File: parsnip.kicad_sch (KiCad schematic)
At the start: 67 parts, among them J1 SPI BUS, J2 I2C3, J3 I2C1, J4 I2C2, J5 e-Ink Display Connector, J6 UART0, SW1 ESP_RESET, SW2 BOOT, U1 ESP32-S3-WROOM-1-N16R8, Y1 32.768KHz

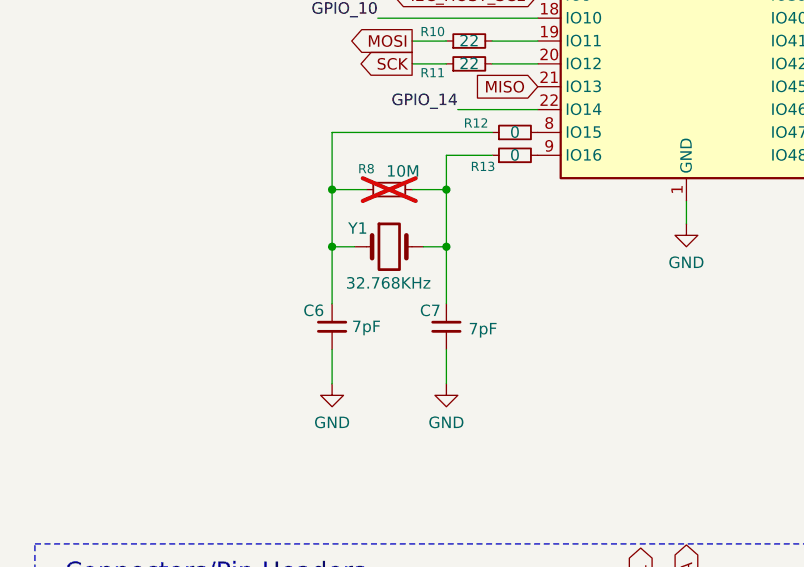
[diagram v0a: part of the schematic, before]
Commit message: organize part fields
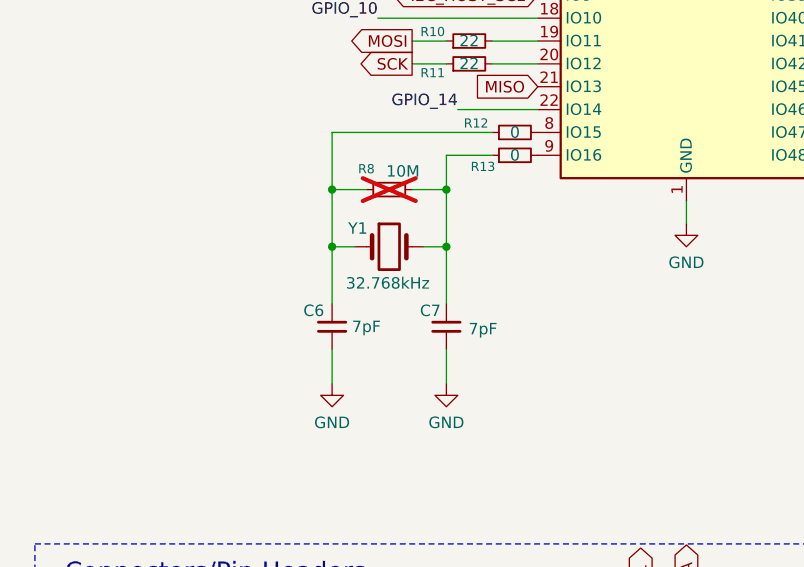
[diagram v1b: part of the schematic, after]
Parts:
- C1, C2, C3, C8: Capacitor Rating X5R -> (none); Dielectric (none) -> X5R; MPN (none) -> HGC0402R5225K350NTEJ; Manufacturer (none) -> Chinocera; Tolerance (none) -> 10%; Voltage Rating 25V -> 35V
- C10, C11: Capacitor Rating X7R -> (none); Dielectric (none) -> X5R; MPN (none) -> TCC0603X5R106M350CT; Manufacturer (none) -> CCTC; Tolerance (none) -> 20%; Voltage Rating 16V -> 35V
- C13: Dielectric (none) -> X5R; MPN (none) -> HGC0402R5225K350NTEJ; Manufacturer (none) -> Chinocera; Tolerance (none) -> 10%; Voltage Rating 16V -> 35V
- C14: Dielectric (none) -> X5R; MPN (none) -> CGA0805X5R106M500MT; Manufacturer (none) -> HRE; Tolerance (none) -> 20%; Voltage Rating 25V -> 50V
- C17: Dielectric (none) -> X7R; MPN (none) -> TCC0402X7R105K250AT; Manufacturer (none) -> CCTC; Tolerance (none) -> 10%; Voltage Rating 16V -> 25V
- C182: Capacitor Rating X7R -> (none); Dielectric (none) -> X7R; MPN (none) -> TCC0402X7R105K250AT; Manufacturer (none) -> CCTC; Tolerance (none) -> 10%
- C5: Capacitor Rating X7R -> (none); Dielectric (none) -> X7R; MPN (none) -> 0402B104J500NT; Manufacturer (none) -> FH (Fenghua); Tolerance (none) -> 5%
- C6, C7: Dielectric (none) -> C0G; MPN (none) -> FN15N7R0D500PNG; Manufacturer (none) -> PSA (Prosperity Dielectrics); Voltage Rating (none) -> 50V
- D1: Manufacturer ti -> Texas Instruments
- D2, D3: Manufacturer (none) -> Texas Instruments
- D4: MPN (none) -> 1N5819WS; Manufacturer (none) -> Hottech
- F1, F3: value 1A Hold -> 1A hold; MPN (none) -> ASMD0805-100; Manufacturer (none) -> JDT
- F2: value 2A Hold, 4A Trip -> 2A hold; MPN (none) -> SL0805200-12V; Manufacturer (none) -> TECHFUSE
- F4: value SMD0805B035TF -> 350mA hold; MPN (none) -> SMD0805B035TF; Manufacturer (none) -> Brightking
- J1: MPN (none) -> HX PM2.54-1x6P WT; Manufacturer (none) -> HANXIA
- J2: MPN (none) -> SM04B-SRSS-TB(LF)(SN); Manufacturer (none) -> JST
- J3: MPN (none) -> HX PM2.54-1x4P WT; Manufacturer (none) -> HANXIA
- J5: MPN (none) -> WAFER-MX1.25-8PWB; Manufacturer (none) -> XUNPU
- J6: MPN (none) -> SM03B-SRSS-TB(LF)(SN); Manufacturer (none) -> JST
- R1, R2, R3, R4: MPN (none) -> 1RC0402F3309; Manufacturer (none) -> SAE; Power Rating (none) -> 62.5mW; Tolerance (none) -> 1%
- R10, R11, R16, R17: MPN (none) -> ARG02DTC0220; Manufacturer (none) -> Viking Tech; Power Rating (none) -> 62.5mW; Tolerance (none) -> 0.5%
- R12, R13, R14, R15, R18, R19, R5, R6: MPN (none) -> CRCW04020000Z0EDHP; Manufacturer (none) -> Vishay
- R20, R24, R25, R26, R7, R9: MPN (none) -> FRH0402D1002TS; Manufacturer (none) -> FOJAN; Power Rating (none) -> 62.5mW; Tolerance (none) -> 0.5%
- R21, R22: MPN (none) -> TC0225B2201TCC; Manufacturer (none) -> UNI-ROYAL; Power Rating (none) -> 62.5mW; Tolerance (none) -> 0.1%
- R23: MPN (none) -> ARG02BTC1003; Manufacturer (none) -> Viking Tech; Power Rating (none) -> 62.5mW; Tolerance (none) -> 0.1%
- R8: LCSC Part C54102219 -> C273584; MPN (none) -> RS-05L1005FT; Manufacturer (none) -> FH (Fenghua); Power Rating (none) -> 125mW; Tolerance (none) -> 1%
- SW1, SW2: MPN (none) -> SKRKAHE020; Manufacturer (none) -> Alps Alpine
- U1: MPN (none) -> ESP32-S3-WROOM-1-N16R8; Manufacturer (none) -> Espressif Systems
- Y1: value 32.768KHz -> 32.768kHz; MPN (none) -> 3131M-32.768DT06LL-R50L; Manufacturer (none) -> HCI

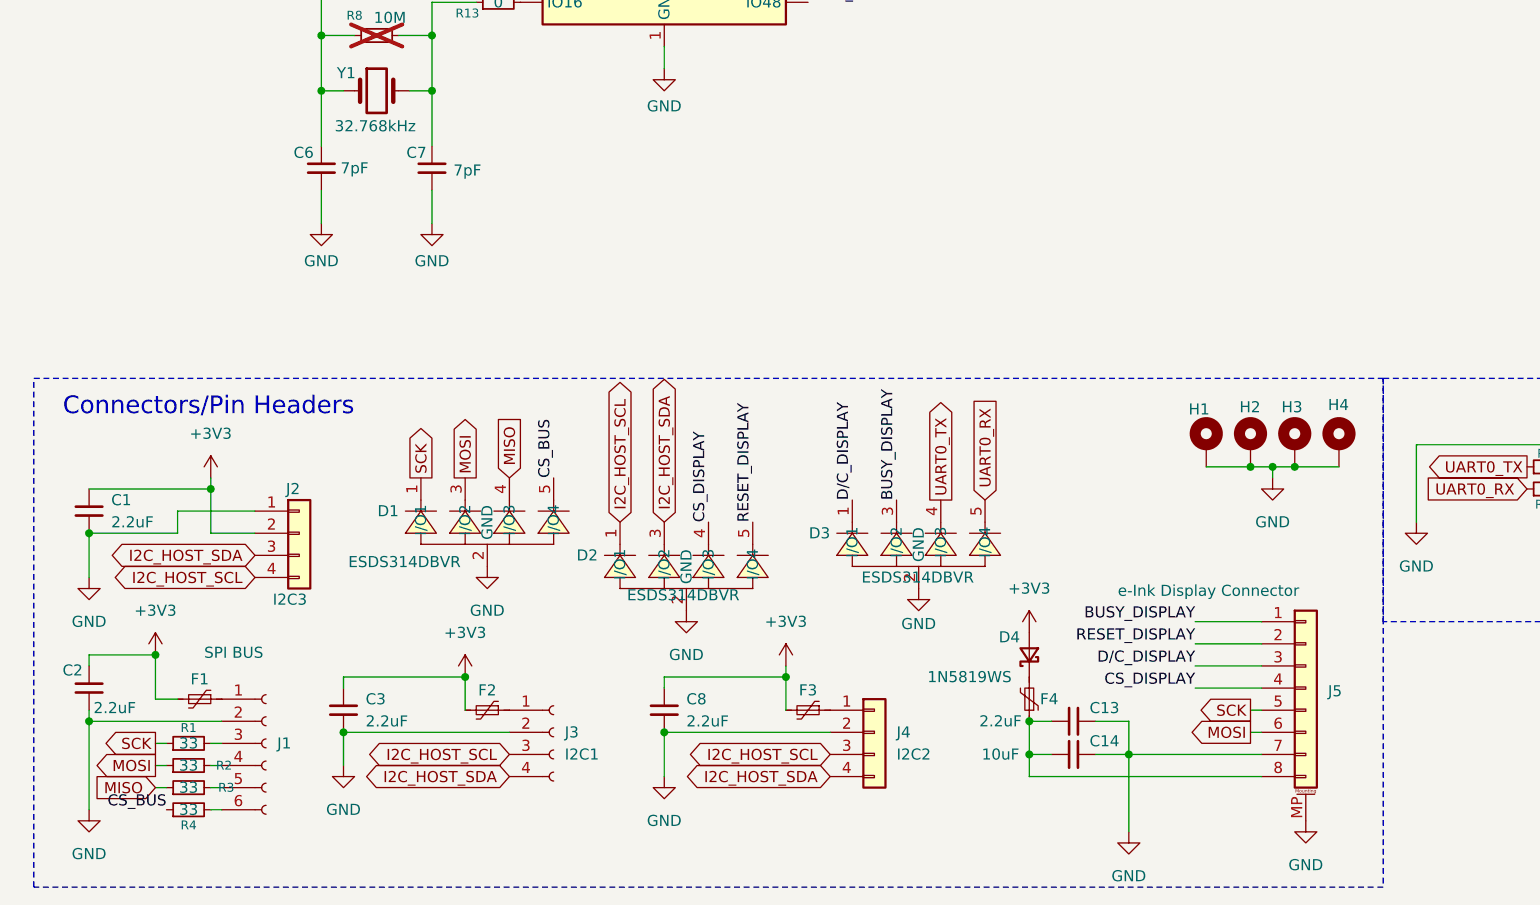
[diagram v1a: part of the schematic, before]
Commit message: add extra PWR_FLAGs
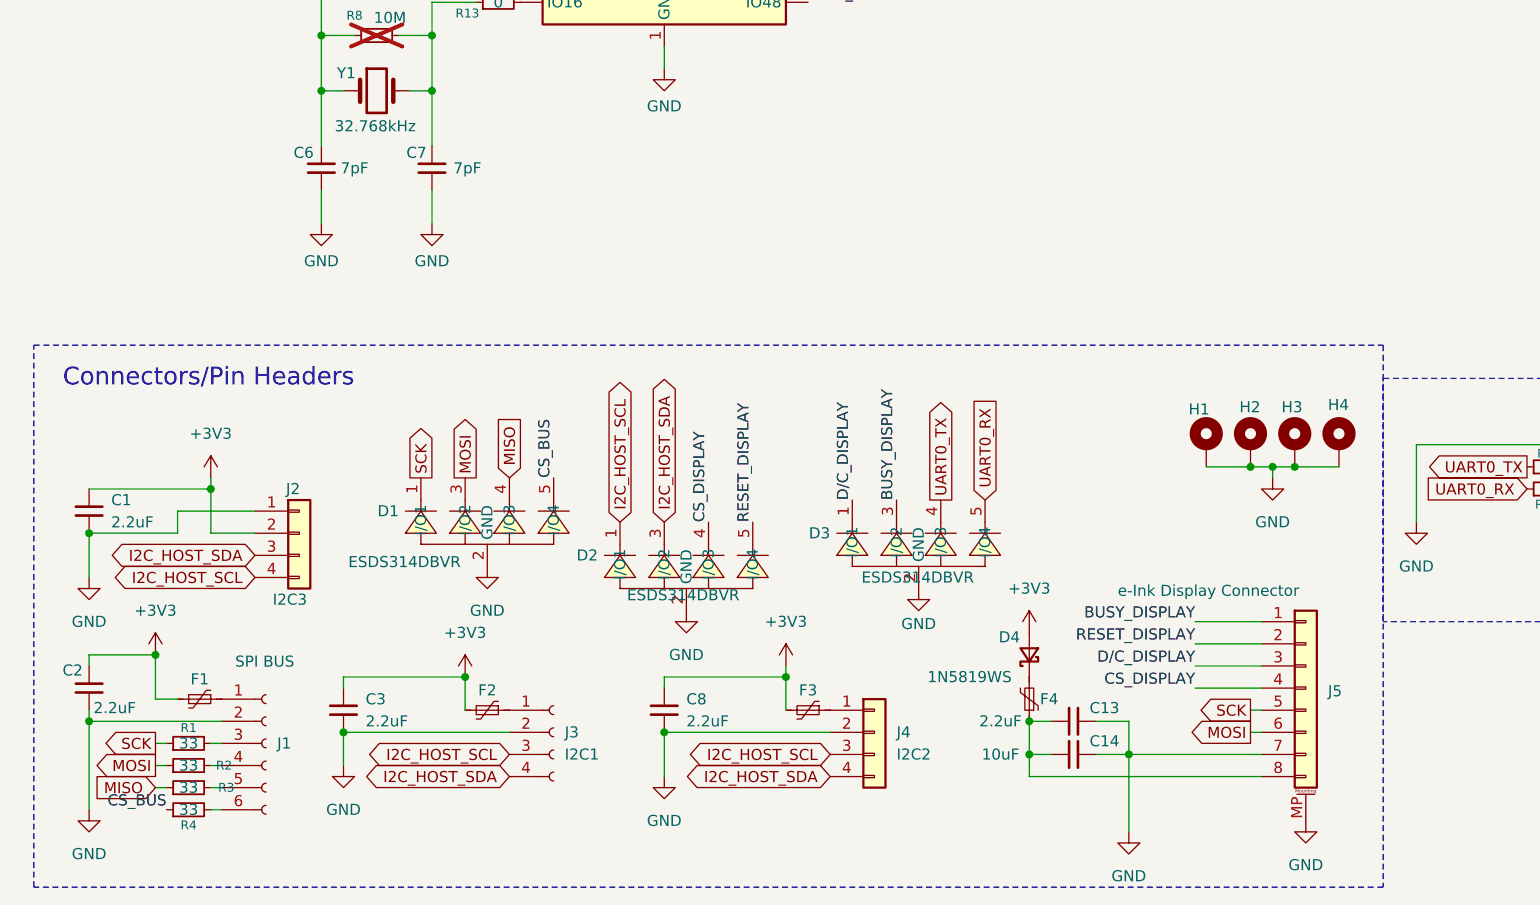
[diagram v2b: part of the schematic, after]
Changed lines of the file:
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@@
 	)
 	(rectangle
-		(start 16.51 137.16)
+		(start 16.51 133.35)
 		(end 171.45 195.58)
 		(stroke
@@
 	(text "Connectors/Pin Headers"
 		(exclude_from_sim no)
-		(at 36.576 140.462 0)
+		(at 36.576 137.16 0)
 		(effects
 			(font
@@
 		)
 		(property "Value" "SPI BUS"
-			(at 36.068 168.656 0)
+			(at 39.624 169.672 0)
 			(show_name no)
 			(do_not_autoplace no)
@@
 		)
 		(property "Value" "7pF"
-			(at 66.294 113.284 0)
+			(at 66.294 113.03 0)
 			(show_name no)
 			(do_not_autoplace no)
